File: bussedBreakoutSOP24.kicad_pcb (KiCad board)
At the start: 2 copper layers, 2.9 x 2.9 mm, 51 parts, among them J1 Conn_01x12_Pin, J10 Conn_01x06_Pin, J11 Conn_01x06_Pin, J12 Conn_01x06_Pin, J13 Conn_01x06_Pin, J14 Conn_01x06_Pin, J15 Conn_01x06_Pin, J16 Conn_01x06_Pin, J17 Conn_01x06_Pin, J18 Conn_01x06_Pin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

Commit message: Change to a SOP24 breakout
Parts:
- removed J26, J27: Conn_01x06_Pin, SMD:SMD_0805_grid_1x6
- J21: value SSOP-24 -> SOP-24; footprint SMD:SSOP-24_3.9-7.5mmx8.2mm_P0.65mm -> SMD:SOP-24_3.9-7.5mmx15.4mm_P1.27mm
- moved J24 17.8 mm to (33.0, 52.1)
- moved J25 5.08 mm to (33.0, 54.6)
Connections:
- J22 pad 5: GND -> unconnected-(J22-Pin_5-Pad5)
- J22 pad 6: GND -> unconnected-(J22-Pin_6-Pad6)
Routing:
- net GND: track 46.8 -> 52.1 mm
- net VCC: track 47.9 -> 53.2 mm
- net /13: track 19.8 -> 15.3 mm
- net /1: track 20.0 -> 15.5 mm
- net /12: track 20.1 -> 16.1 mm
- net /24: track 19.8 -> 15.7 mm
- net /14: track 18.0 -> 15.1 mm
- net /23: track 18.0 -> 15.1 mm
- net /2: track 18.0 -> 15.1 mm
- net /11: track 18.0 -> 15.1 mm
- net /5: track 14.3 -> 11.9 mm
- net /15: track 16.1 -> 13.8 mm
- net /10: track 16.1 -> 13.9 mm
- net /3: track 16.1 -> 13.8 mm
- net /22: track 16.1 -> 13.8 mm
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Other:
- board text added: "1.27mm pitch"
- board text added: "SOP-24"
- board text removed: "0.65mm pitch"
- board text removed: "SSOP-24"

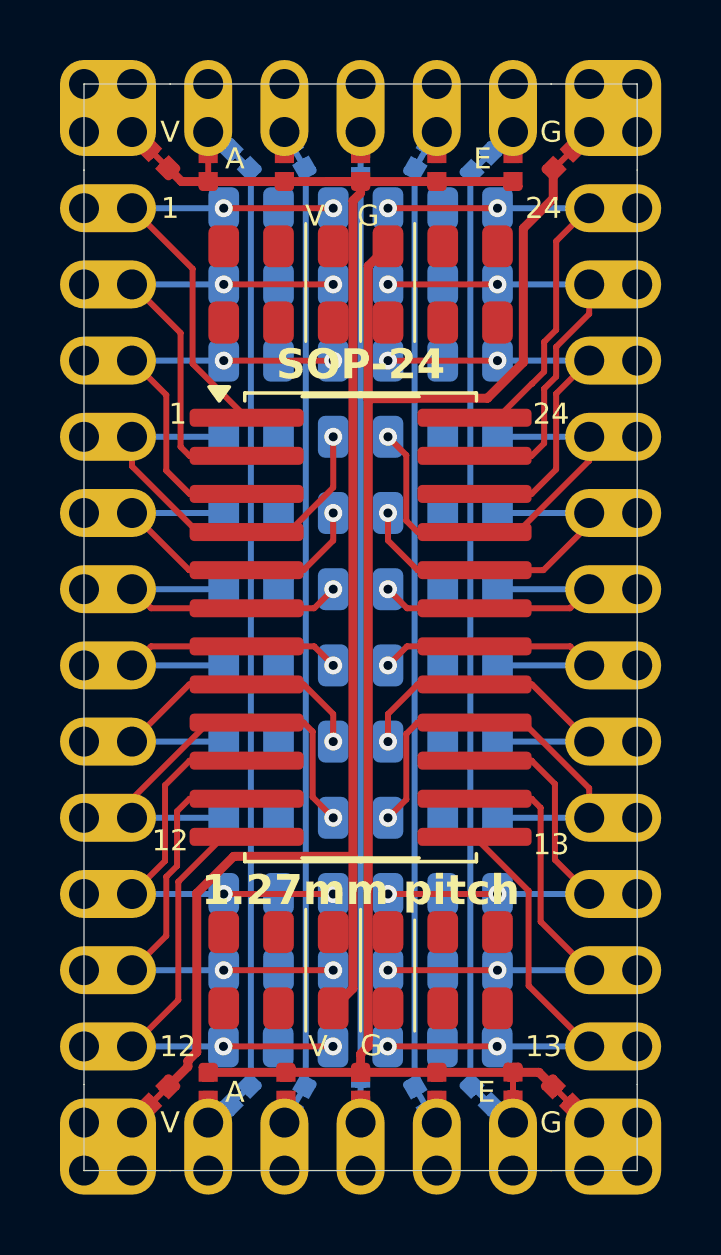
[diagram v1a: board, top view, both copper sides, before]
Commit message: Change prototype area 0402s and connect it to VCC+GND+middle rows of pads on bottom
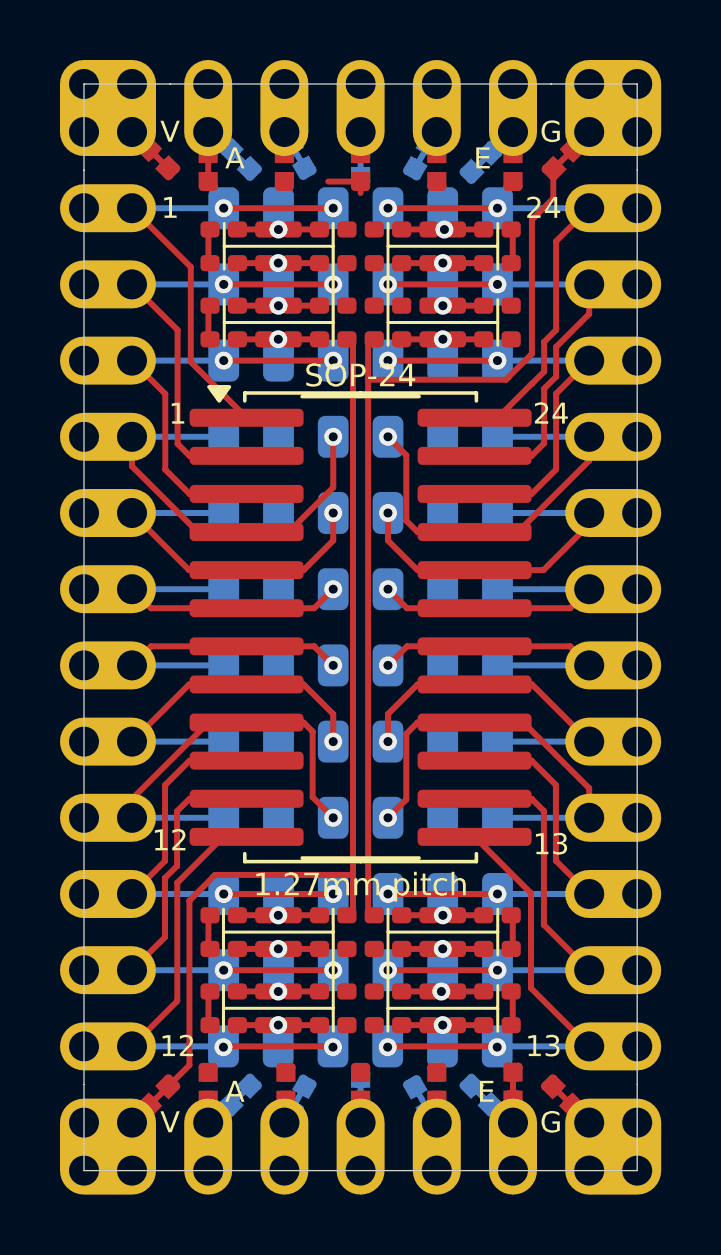
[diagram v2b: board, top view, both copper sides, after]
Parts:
- J22, J23, J24, J25: value Conn_01x06_Pin -> Conn_01x24_Pin; footprint SMD:SMD_0805_grid_1x6 -> SMD:SMD_grid_2x12_0402
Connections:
- J10 pad 2: unconnected-(J10-Pin_2-Pad2) -> /2T
- J10 pad 5: unconnected-(J10-Pin_5-Pad5) -> /23T
- J11 pad 2: unconnected-(J11-Pin_2-Pad2) -> /3T
- J11 pad 5: unconnected-(J11-Pin_5-Pad5) -> /22T
- J18 pad 2: unconnected-(J18-Pin_2-Pad2) -> /10T
- J18 pad 5: unconnected-(J18-Pin_5-Pad5) -> /15T
- J19 pad 2: unconnected-(J19-Pin_2-Pad2) -> /11T
- J19 pad 5: unconnected-(J19-Pin_5-Pad5) -> /14T
- J20 pad 2: unconnected-(J20-Pin_2-Pad2) -> /12T
- J20 pad 5: unconnected-(J20-Pin_5-Pad5) -> /13T
- J22 pad 1: unconnected-(J22-Pin_1-Pad1) -> Net-(J22-Pin_1)
- J22 pad 2: unconnected-(J22-Pin_2-Pad2) -> Net-(J22-Pin_1)
- J22 pad 3: VCC -> /1T
- J22 pad 4: GND -> /2T
- J22 pad 5: unconnected-(J22-Pin_5-Pad5) -> /1T
- J22 pad 6: unconnected-(J22-Pin_6-Pad6) -> /2T
- J23 pad 1: unconnected-(J23-Pin_1-Pad1) -> Net-(J23-Pin_1)
- J23 pad 2: unconnected-(J23-Pin_2-Pad2) -> Net-(J23-Pin_1)
- J23 pad 3: VCC -> /2T
- J23 pad 4: GND -> /3T
- J23 pad 5: unconnected-(J23-Pin_5-Pad5) -> /2T
- J23 pad 6: unconnected-(J23-Pin_6-Pad6) -> /3T
- J24 pad 1: unconnected-(J24-Pin_1-Pad1) -> Net-(J24-Pin_1)
- J24 pad 2: unconnected-(J24-Pin_2-Pad2) -> Net-(J24-Pin_1)
- J24 pad 3: VCC -> /10T
- J24 pad 4: GND -> /11T
- J24 pad 5: unconnected-(J24-Pin_5-Pad5) -> /10T
- J24 pad 6: unconnected-(J24-Pin_6-Pad6) -> /11T
- J25 pad 1: unconnected-(J25-Pin_1-Pad1) -> Net-(J25-Pin_1)
- J25 pad 2: unconnected-(J25-Pin_2-Pad2) -> Net-(J25-Pin_1)
- J25 pad 3: VCC -> /11T
- J25 pad 4: GND -> /12T
- J25 pad 5: unconnected-(J25-Pin_5-Pad5) -> /11T
- J25 pad 6: unconnected-(J25-Pin_6-Pad6) -> /12T
- J9 pad 2: unconnected-(J9-Pin_2-Pad2) -> /1T
- J9 pad 5: unconnected-(J9-Pin_5-Pad5) -> /24T
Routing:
- net /11T: track 0.00 -> 3.73 mm, vias 0 -> 2
- net /2T: track 0.00 -> 3.73 mm, vias 0 -> 2
- net /14T: track 0.00 -> 3.69 mm, vias 0 -> 2
- net /23T: track 0.00 -> 2.93 mm, vias 0 -> 2
- net /15T: track 0.00 -> 2.13 mm, vias 0 -> 1
- net /22T: track 0.00 -> 2.13 mm, vias 0 -> 1
- net /3T: track 0.00 -> 2.12 mm, vias 0 -> 1
- net /10T: track 0.00 -> 2.12 mm, vias 0 -> 1
- net /24T: track 0.00 -> 1.61 mm, vias 0 -> 1
- net /1T: track 0.00 -> 1.61 mm, vias 0 -> 1
- net /13T: track 0.00 -> 1.43 mm, vias 0 -> 1
- net /12T: track 0.00 -> 1.43 mm, vias 0 -> 1
- net Net-(J25-Pin_23): track 0.00 -> 1.12 mm
- net Net-(J25-Pin_1): track 0.00 -> 1.12 mm
- net Net-(J24-Pin_23): track 0.00 -> 1.12 mm
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
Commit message: Reoriente power distribution jumpers to remove GND/VCC routing workaround
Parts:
- moved JP17 1.10 mm to (32.0, 26.2), turned to 45 degrees
- moved JP16 1.10 mm to (29.5, 26.2), turned to 45 degrees
- moved JP18 1.01 mm to (34.6, 26.2), turned to 45 degrees
- moved JP19 1.01 mm to (37.2, 26.2), turned to 45 degrees
- moved JP23 1.00 mm to (36.4, 57.7), turned to -135 degrees
- moved JP21 0.99 mm to (31.4, 57.6), turned to -135 degrees
- moved JP24 0.98 mm to (39.0, 57.5), turned to -135 degrees
- moved JP20 0.95 mm to (28.8, 57.5), turned to -135 degrees
- moved JP15 0.94 mm to (27.1, 26.3), turned to 45 degrees
- moved JP22 0.92 mm to (33.9, 57.6), turned to -135 degrees
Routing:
- net VCC: track 53.3 -> 51.8 mm
- net /10T: track 2.12 -> 1.31 mm
